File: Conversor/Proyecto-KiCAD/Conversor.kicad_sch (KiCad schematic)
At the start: 22 parts, among them J1 ConnPila, J2 ConnTrafoP, J3 ConnTrafoS, J4 ConnLf, J5 ConnCarga, Q1 IRFP150, Q2 IRFP150, Q3 IRFP150, Q4 IRFP150

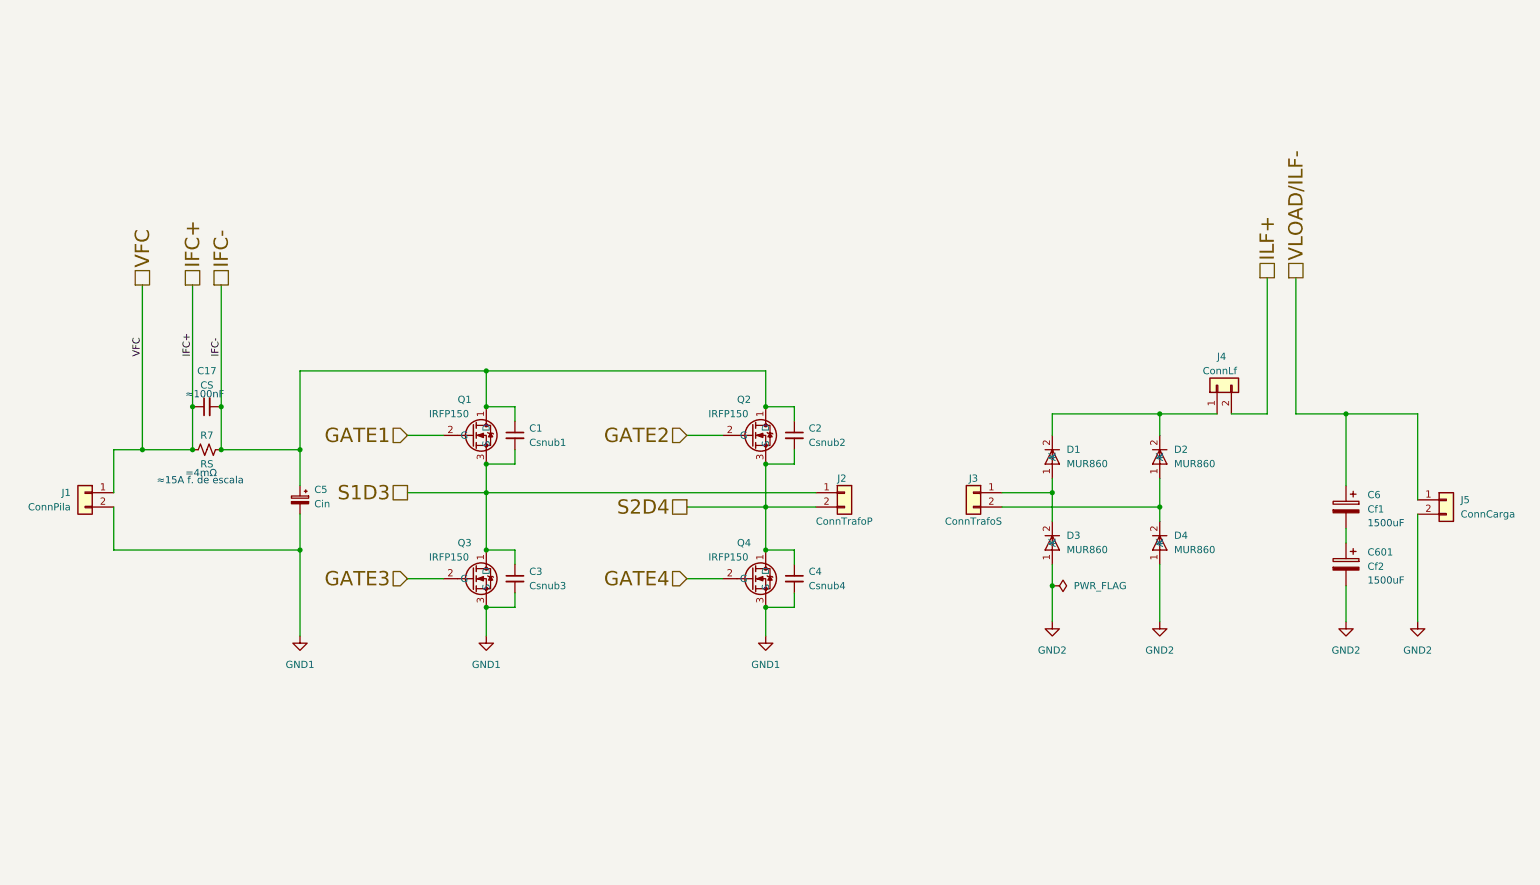
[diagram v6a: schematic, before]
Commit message: Agregar el selector de alim. de 12V y seguir emprolijando la placa
- Agregar modelos de los switches
- Agregar algunos test points
Por hacer:
  - Todo lo de los dos anteriores commits
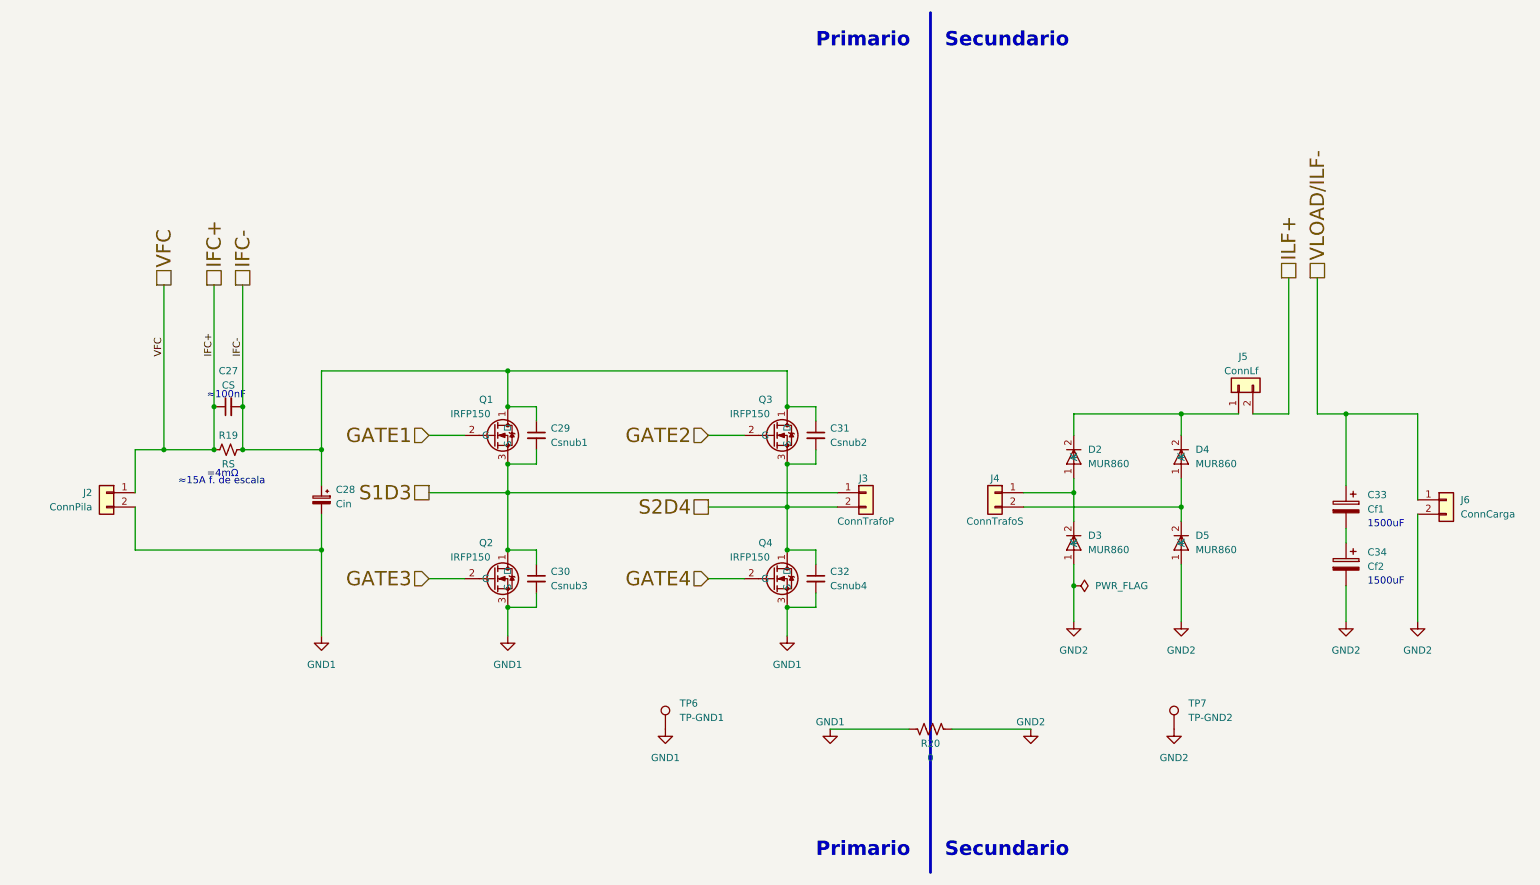
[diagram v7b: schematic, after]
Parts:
- added R20: 0, Resistor_SMD:R_1206_3216Metric_Pad1.30x1.75mm_HandSolder, symbol Device:R_US
- added TP6: TP-GND1, TestPoint:TestPoint_THTPad_2.0x2.0mm_Drill1.0mm, symbol Connector:TestPoint
- added TP7: TP-GND2, TestPoint:TestPoint_THTPad_2.0x2.0mm_Drill1.0mm, symbol Connector:TestPoint
- renumbered C17 to C27, C5 to C28, C1 to C29, C3 to C30, C2 to C31, C4 to C32, C6 to C33, C601 to C34, D1 to D2, D2 to D4, D4 to D5, J1 to J2, J2 to J3, J3 to J4, J4 to J5, J5 to J6, Q3 to Q2, Q2 to Q3, R7 to R19
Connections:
- net GND1: now also R20.2, TP6.1
- net GND2: now also R20.1, TP7.1
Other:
- note added: "Primario"
- note added: "Secundario"
- moved on the sheet: C27, C28, C29, C30, C31, C32, D2, D3, D4, D5, J2, J3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

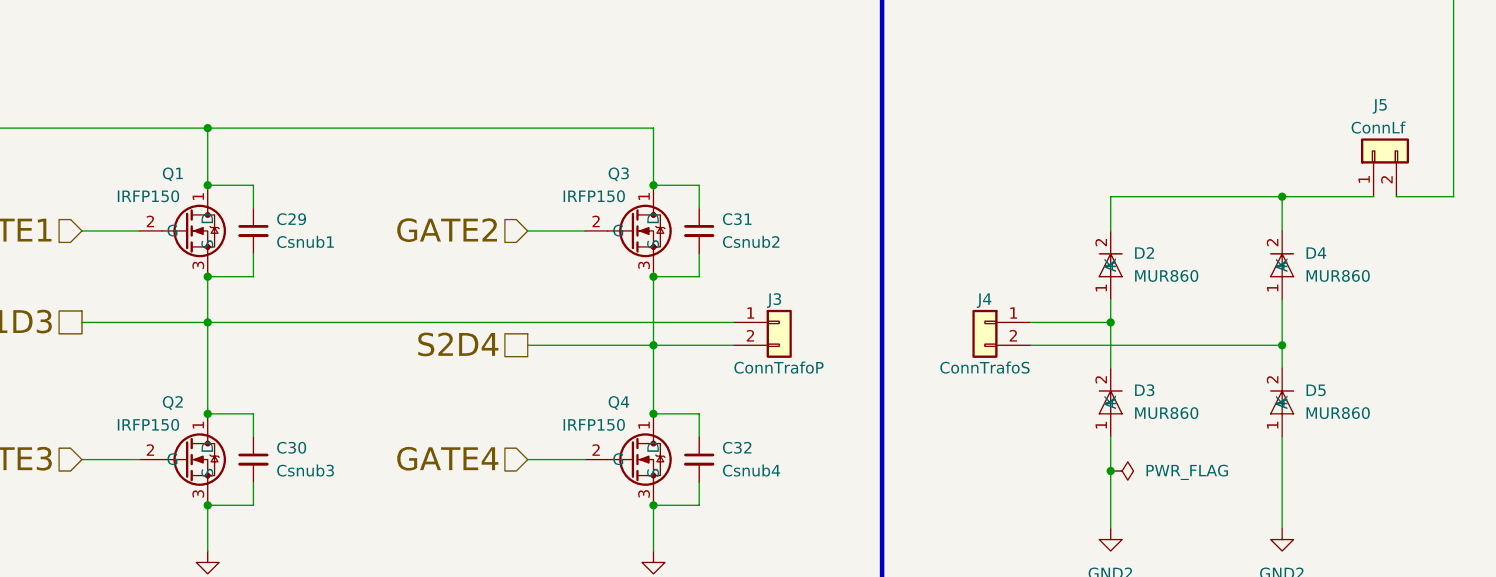
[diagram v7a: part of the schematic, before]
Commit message: Emprolijar la PCB
- Agregar logo de FI
- Redondear pistas faltantes
- Aumentar la distancia del cobre al borde
- acraca racuca
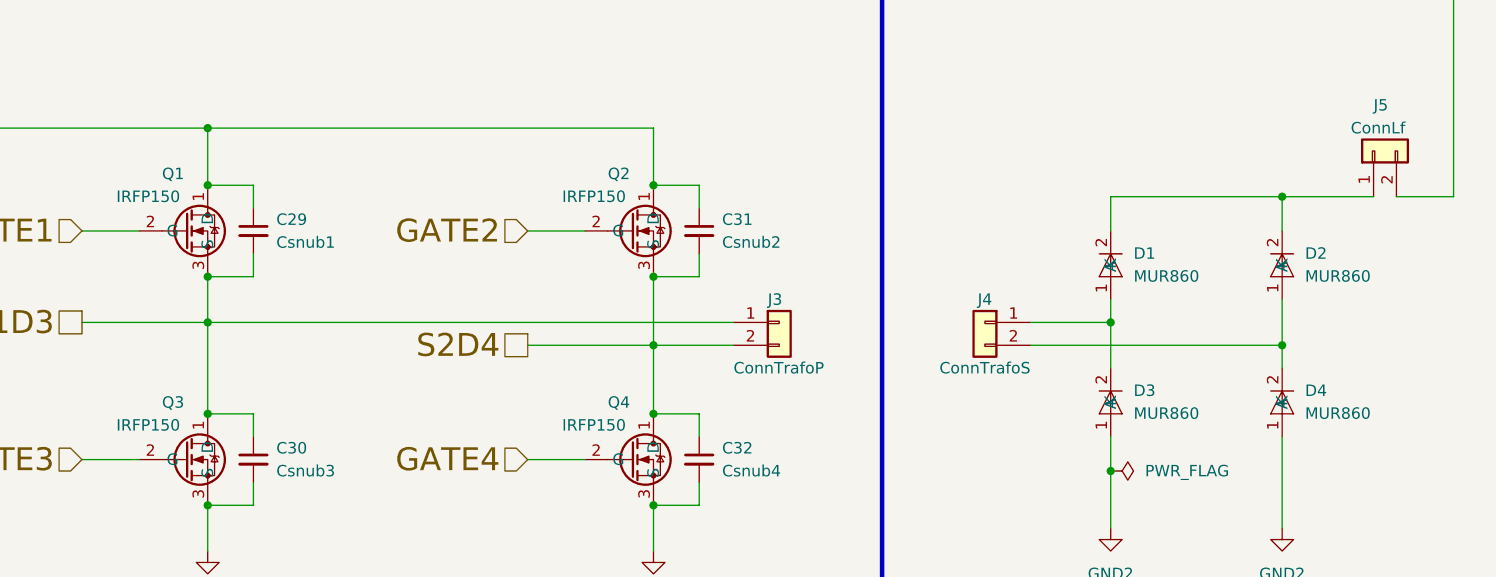
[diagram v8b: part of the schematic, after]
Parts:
- renumbered D2 to D1, D4 to D2, D5 to D4, Q3 to Q2, Q2 to Q3
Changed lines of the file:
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@@
   (symbol (lib_name "MUR860_1") (lib_id "Componentes proyecto:MUR860") (at 204.47 91.44 0) (unit 1)
     (in_bom yes) (on_board yes) (fields_autoplaced)
-    (property "Reference" "D2" (id 0) (at 207.01 90.1318 0)
+    (property "Reference" "D1" (id 0) (at 207.01 90.1318 0)
       (effects (font (size 1.27 1.27)) (justify left))
     )
@@
   (symbol (lib_name "MUR860_2") (lib_id "Componentes proyecto:MUR860") (at 223.52 91.44 0) (unit 1)
     (in_bom yes) (on_board yes) (fields_autoplaced)
-    (property "Reference" "D4" (id 0) (at 226.06 90.1318 0)
+    (property "Reference" "D2" (id 0) (at 226.06 90.1318 0)
       (effects (font (size 1.27 1.27)) (justify left))
     )
@@
   (symbol (lib_id "Componentes proyecto:IRFP150") (at 153.67 86.36 0) (unit 1)
     (in_bom yes) (on_board yes)
-    (property "Reference" "Q3" (id 0) (at 148.59 81.28 0)
+    (property "Reference" "Q2" (id 0) (at 148.59 81.28 0)
       (effects (font (size 1.27 1.27)) (justify left))
     )
@@
   (symbol (lib_name "MUR860_3") (lib_id "Componentes proyecto:MUR860") (at 223.52 106.68 0) (unit 1)
     (in_bom yes) (on_board yes) (fields_autoplaced)
-    (property "Reference" "D5" (id 0) (at 226.06 105.3718 0)
+    (property "Reference" "D4" (id 0) (at 226.06 105.3718 0)
       (effects (font (size 1.27 1.27)) (justify left))
     )
@@
   (symbol (lib_id "Componentes proyecto:IRFP150") (at 104.14 111.76 0) (unit 1)
     (in_bom yes) (on_board yes)
-    (property "Reference" "Q2" (id 0) (at 99.06 106.68 0)
-      (effects (font (size 1.27 1.27)) (justify left))
-    )
+    (property "Reference" "Q3" (id 0) (at 99.06 106.68 0)
+      (effects (font (size 1.27 1.27)) (justify left))
+    )
